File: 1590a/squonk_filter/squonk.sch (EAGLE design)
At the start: 38 parts, among them IC1 TL072, Q1 MPF102, Q2 2N4123

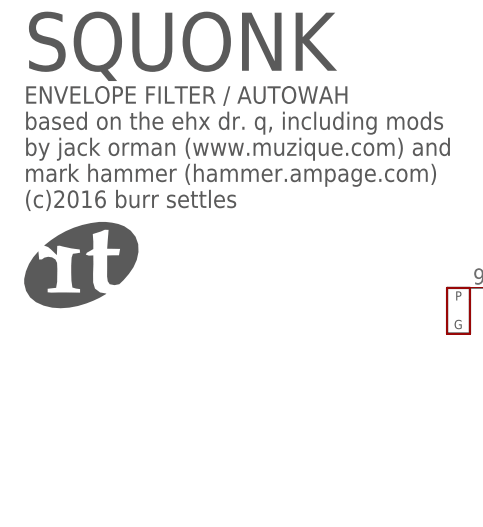
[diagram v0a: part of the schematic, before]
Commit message: updated library + logos
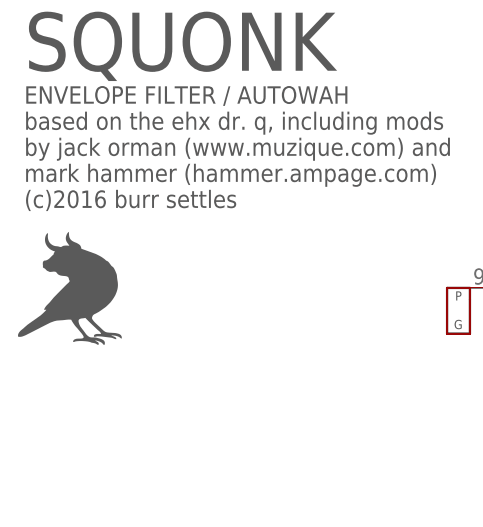
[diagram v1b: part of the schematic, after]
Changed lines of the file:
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@@
 <setting verticaltext="up"/>
 </settings>
-<grid distance="0.05" unitdist="inch" unit="inch" style="lines" multiple="2" display="no" altdistance="0.01" altunitdist="inch" altunit="inch"/>
+<grid distance="0.1" unitdist="inch" unit="inch" style="lines" multiple="1" display="no" altdistance="0.01" altunitdist="inch" altunit="inch"/>
 <layers>
 <layer number="1" name="Top" color="4" fill="1" visible="no" active="no"/>
@@
 <part name="R1" library="resistors" deviceset="R_" device=".3B" value="1M"/>
 <part name="GND1" library="supply pins" deviceset="GND" device=""/>
-<part name="U$2" library="logos" deviceset="REBELSTRUST" device=""/>
+<part name="BF1" library="logos" deviceset="BULLFINCH" device=""/>
 </parts>
 <sheets>
@@
 <instance part="R1" gate="G$1" x="27.94" y="77.47" rot="R90"/>
 <instance part="GND1" gate="GND" x="27.94" y="69.85"/>
-<instance part="U$2" gate="G$1" x="2.54" y="22.86"/>
+<instance part="BF1" gate="G$1" x="7.62" y="25.4"/>
 </instances>
 <busses>
